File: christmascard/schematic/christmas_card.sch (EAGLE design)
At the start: 85 parts, among them IC1 WS2811-SOP8, IC2 WS2811-SOP8, IC4 LM1117, IC5 WS2811-SOP8, IC6 MEGA8-AI, Q1 MOSFET-NCHANNELSMD, Q10 TRANSISTOR_PNPSMD, Q11 TRANSISTOR_PNPSMD, Q12 TRANSISTOR_PNPSMD, Q2 MOSFET-NCHANNELSMD, Q3 MOSFET-NCHANNELSMD, Q4 MOSFET-NCHANNELSMD, Q5 TRANSISTOR_PNPSMD, Q9 TRANSISTOR_PNPSMD, X2 USB-MICROB

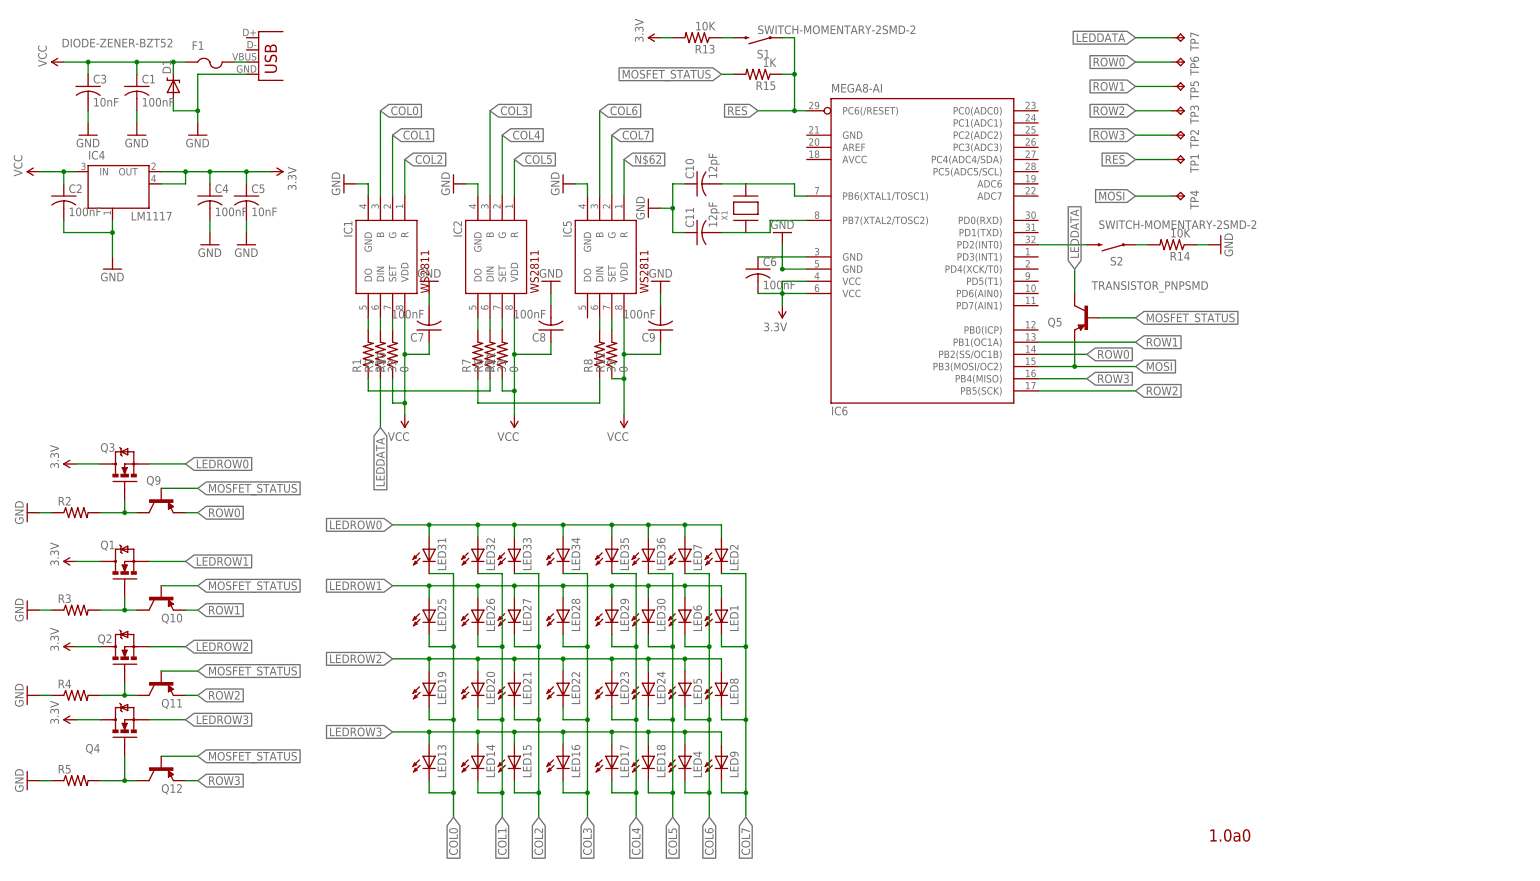
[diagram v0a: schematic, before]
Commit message: Relocated files, removed unused files, updated christmas and clock board and other changes
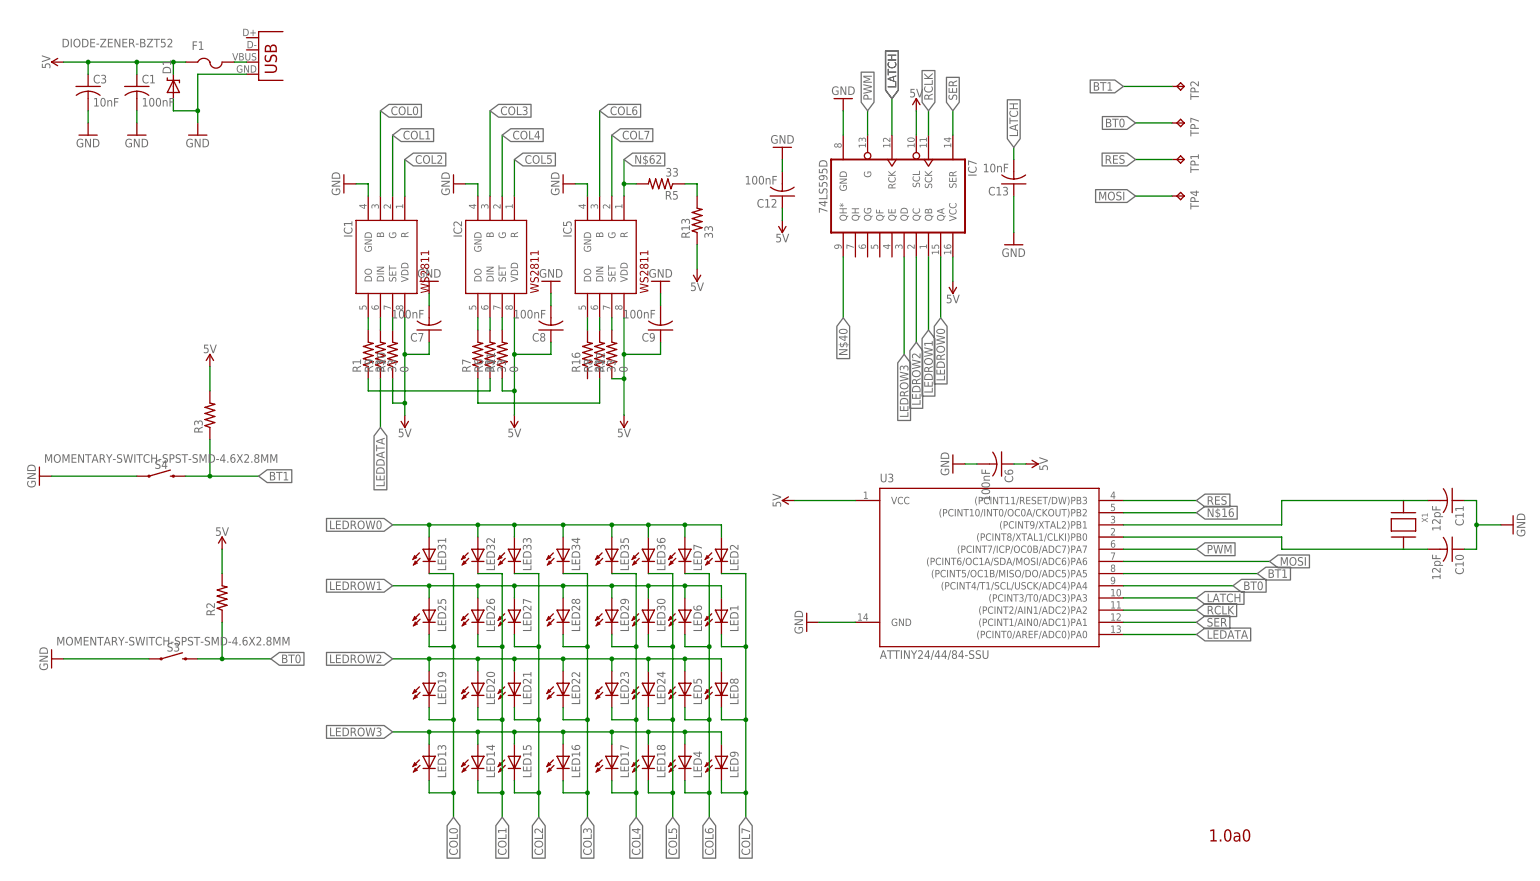
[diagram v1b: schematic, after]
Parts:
- removed C2, C4: 100nF, adafruit:C-USC0603
- removed C5: 10nF, adafruit:C-USC0603
- removed IC4: LM1117, voltage_regulators:LM1117
- removed IC6: MEGA8-AI, atmel:MEGA8-AI
- removed Q1, Q2, Q3, Q4: MOSFET-NCHANNELSMD, SparkFun:MOSFET-NCHANNELSMD
- removed Q10, Q11, Q12, Q5, Q9: TRANSISTOR_PNPSMD, SparkFun:TRANSISTOR_PNPSMD
- removed R14: 10K, adafruit:R-US_R0603
- removed R15: 1K, adafruit:R-US_R0603
- removed R4: (no value), adafruit:R-US_R0603
- removed S1, S2: SWITCH-MOMENTARY-2SMD-2, SparkFun:SWITCH-MOMENTARY-2SMD-2
- removed TP3, TP5, TP6: TPB1,27, testpad:TPB1,27
- added C12: 100nF, adafruit:C-USC0603
- added C13: 10nF, adafruit:C-USC0603
- added IC7: 74LS595D, SparkFun:74LS595D
- added R16: 33, adafruit:R-US_R0603
- added S3, S4: MOMENTARY-SWITCH-SPST-SMD-4.6X2.8MM, SparkFun-Switches:MOMENTARY-SWITCH-SPST-SMD-4.6X2.8MM
- added U3: ATTINY24/44/84-SSU, bt_avr:ATTINY24/44/84-SSU
- R13: value 10K -> 33
- R5: value (none) -> 33
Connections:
- removed net 3.3V: C4.1, C5.1, C6.2, IC4.OUT, IC4.OUT@1, IC6.VCC@1, IC6.VCC@2, Q1.D, Q2.D, Q3.D, Q4.D, R13.2
- removed net MOSFET_STATUS: Q10.B, Q11.B, Q12.B, Q5.B, Q9.B, R15.2
- removed net N$13: Q3.G, Q9.C, R2.2
- removed net N$9: R13.1, S1.2
- removed net ROW0: IC6.PB2(SS/OC1B), Q9.E, TP6.TP
- removed net ROW1: IC6.PB1(OC1A), Q1.G, Q10.C, Q10.E, R3.2, TP5.TP
- removed net ROW2: IC6.PB5(SCK), Q11.C, Q11.E, Q2.G, R4.2, TP3.TP
- removed net ROW3: IC6.PB4(MISO), Q12.C, Q12.E, Q4.G, R5.2, TP2.TP
- removed net VCC: C1.1, C2.1, C3.1, C7.1, C8.1, C9.1, D1.C, F1.1, IC1.VDD, IC2.VDD, IC4.IN, IC5.VDD, R10.1, R11.1, R12.1
- new net 5V: C1.1, C12.1, C3.1, C6.1, C7.1, C8.1, C9.1, D1.C, F1.1, IC1.VDD, IC2.VDD, IC5.VDD, IC7.SCL, IC7.VCC, R10.1, R11.1, R12.1, R13.1, R2.2, R3.2, U3.VCC
- new net BT0: R2.1, S3.2, TP7.TP, U3.(PCINT4/T1/SCL/USCK/ADC4)PA4
- new net BT1: R3.1, S4.2, TP2.TP, U3.(PCINT5/OC1B/MISO/DO/ADC5)PA5
- new net LATCH: C13.2, IC7.RCK, U3.(PCINT3/T0/ADC3)PA3
- new net LEDATA: U3.(PCINT0/AREF/ADC0)PA0
- new net N$16: U3.(PCINT10/INT0/OC0A/CKOUT)PB2
- new net N$40: IC7.QH*
- new net PWM: IC7.G, U3.(PCINT7/ICP/OC0B/ADC7)PA7
- new net RCLK: IC7.SCK, U3.(PCINT2/AIN1/ADC2)PA2
- new net SER: IC7.SER, U3.(PCINT1/AIN0/ADC1)PA1
- net GND: now also C12.2, C13.1, C6.2, IC7.GND, S3.1, S4.1, U3.GND; no longer C2.2, C4.2, C5.2, C6.1, IC4.GND/ADJ, IC6.GND@1, IC6.GND@2, R14.1, R2.1, R3.1, R4.1, R5.1
- net LEDDATA: no longer Q5.C, TP7.TP
- net LEDROW0: now also IC7.QA; no longer Q3.S
- net LEDROW1: now also IC7.QB; no longer Q1.S
- net LEDROW2: now also IC7.QC; no longer Q2.S
- net LEDROW3: now also IC7.QD; no longer Q4.S
- net MOSI: now also U3.(PCINT6/OC1A/SDA/MOSI/ADC6)PA6; no longer IC6.PB3(MOSI/OC2), Q5.E
- net N$10: now also U3.(PCINT8/XTAL1/CLKI)PB0; no longer IC6.PB6(XTAL1/TOSC1)
- net N$11: now also IC5.DO, R16.2; no longer IC6.PD2(INT0), S2.2
- net N$12: now also R13.2, R5.1; no longer R14.2, S2.1
- net N$14: now also U3.(PCINT9/XTAL2)PB1; no longer IC6.PB7(XTAL2/TOSC2)
- net N$62: now also R5.2
- net RES: now also U3.(PCINT11/RESET/DW)PB3; no longer IC6.PC6(/RESET), R15.1, S1.1
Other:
- moved on the sheet: C10, C11, C6, R13, R2, R3, R5, TP2, TP7, X1

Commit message: Improvement and other changes
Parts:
- added 5V, GND: WIREPADSMD2,54-5,08, wirepad:WIREPADSMD2,54-5,08
- added D2: (no value), SparkFun-LED:LED0603
- added R4: 480, adafruit:R-US_R0603
- renumbered TP1 to RES, TP2 to MISO, TP4 to MOSI, TP7 to SCK
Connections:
- removed net N$16: U3.(PCINT10/INT0/OC0A/CKOUT)PB2
- removed net N$41: F1.2, X2.VBUS
- new net DEBUGLED0: D2.A, U3.(PCINT10/INT0/OC0A/CKOUT)PB2
- new net N$9: D2.C, R4.2
- new net VCC: 5V.P, F1.2, X2.VBUS
- net GND: now also GND.P, R4.1
